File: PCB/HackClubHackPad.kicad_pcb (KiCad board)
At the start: 2 copper layers, 59.1 x 47 mm, 7 parts, among them J1 Conn_01x04, SW1 SW_Push, SW2 SW_Push, SW3 SW_Push, SW4 RotaryEncoder_Switch, SW5 RotaryEncoder_Switch, U1 Seeed Studio XIAO SAMD21

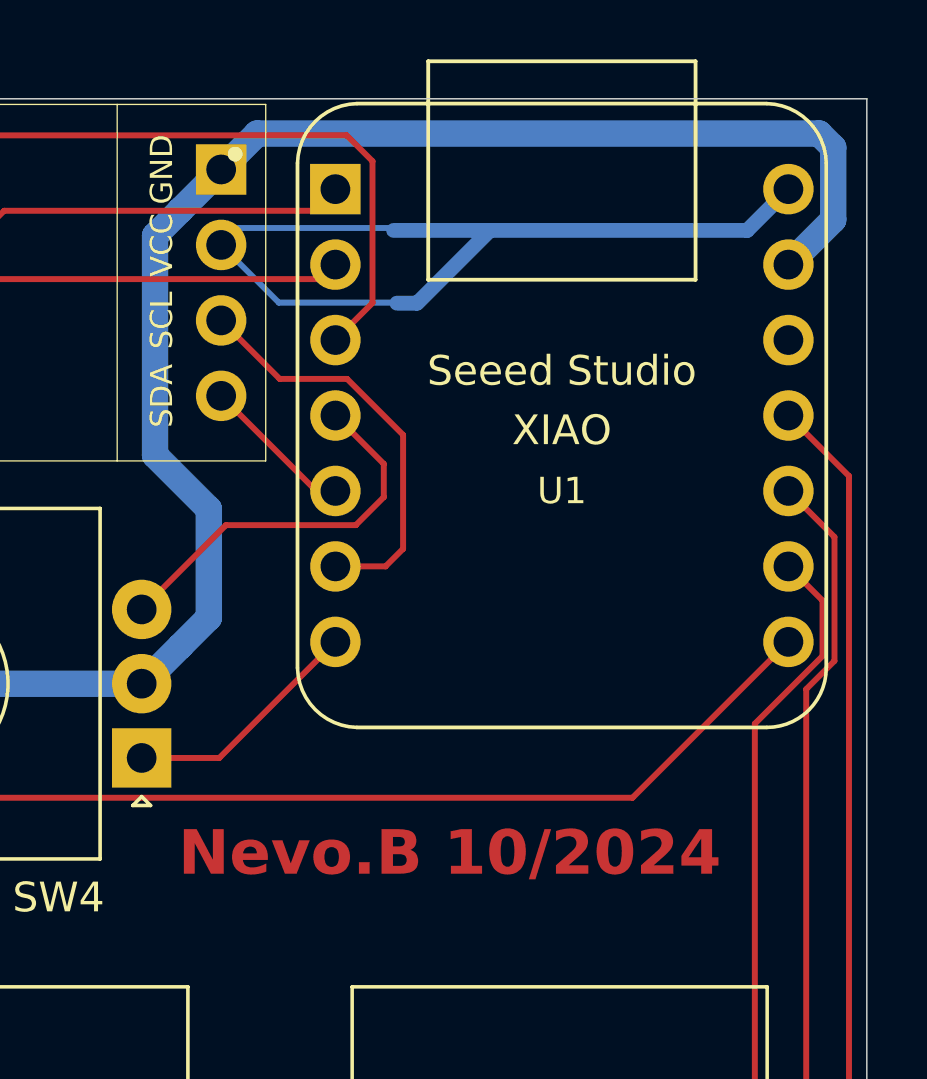
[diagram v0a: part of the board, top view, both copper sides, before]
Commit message: fixed firmware and changed pcb a bit
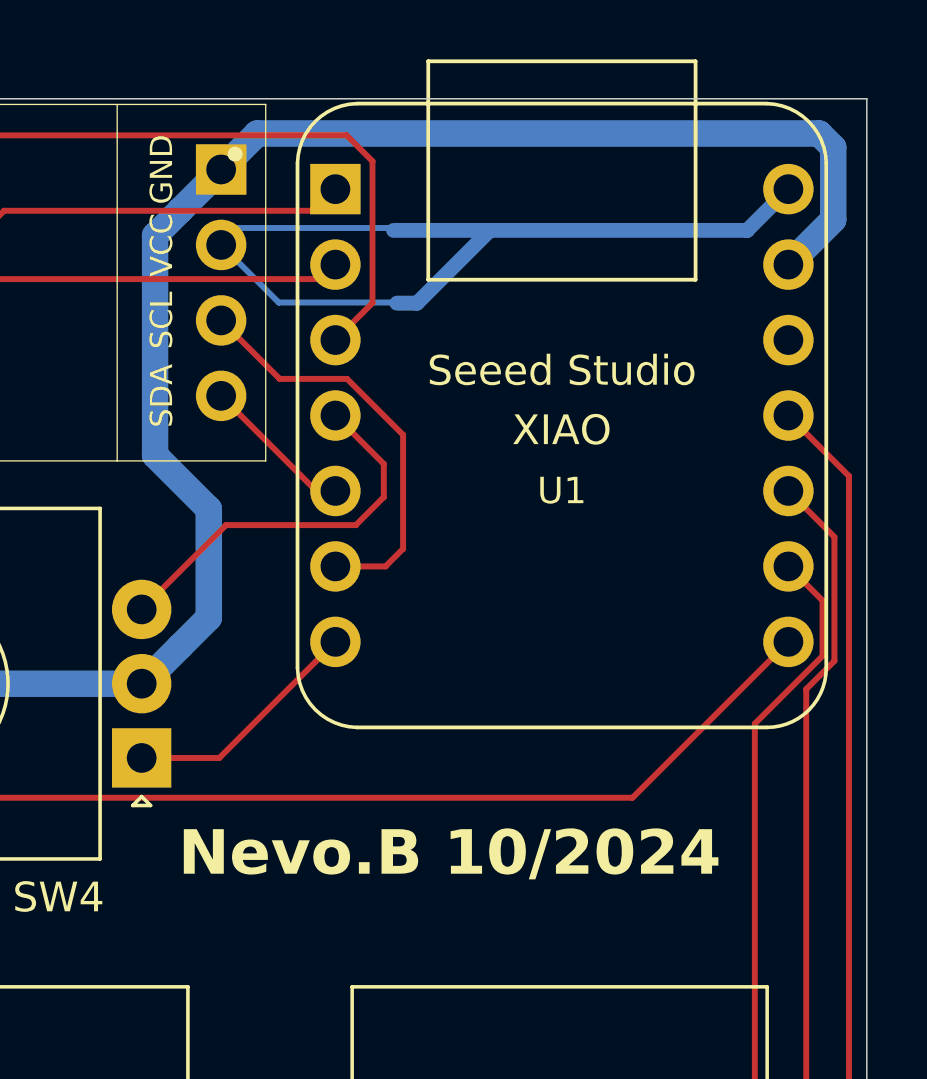
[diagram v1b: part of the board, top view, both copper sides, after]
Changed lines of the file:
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@@
 		(tags "rotary encoder")
 		(property "Reference" "SW5"
-			(at 2.8 -4.7 360)
+			(at 2.8 -4.7 0)
 			(layer "F.SilkS")
 			(effects
@@
 		)
 		(property "Value" "RotaryEncoder_Switch"
-			(at 7.5 10.4 360)
+			(at 7.5 10.4 0)
 			(layer "F.Fab")
 			(effects
@@
 		)
 		(fp_text user "${REFERENCE}"
-			(at 11.1 6.3 360)
+			(at 11.1 6.3 0)
 			(layer "F.Fab")
 			(effects
@@
 		(at 178.64525 33.422015)
 		(property "Reference" "U1"
-			(at 0 2.54 360)
+			(at 0 2.54 0)
 			(layer "F.SilkS")
 			(effects
@@
 		)
 		(property "Value" "Seeed Studio XIAO SAMD21"
-			(at 0 5.08 360)
+			(at 0 5.08 0)
 			(layer "F.SilkS")
 			(hide yes)
@@
 		)
 		(property "Footprint" "Seeed Studio XIAO Series Library:XIAO-Generic-Thruhole-14P-2.54-21X17.8MM"
-			(at 0 0 360)
+			(at 0 0 0)
 			(layer "F.Fab")
 			(hide yes)
@@
 		)
 		(property "Datasheet" ""
-			(at 0 0 360)
+			(at 0 0 0)
 			(layer "F.Fab")
 			(hide yes)
@@
 		)
 		(property "Description" ""
-			(at 0 0 360)
+			(at 0 0 0)
 			(layer "F.Fab")
 			(hide yes)
@@
 		(fp_arc
 			(start 6.9 -10.5)
-			(mid 8.301492 -9.901492)
+			(mid 8.301494 -9.901494)
 			(end 8.9 -8.5)
 			(stroke
@@
 		(tags "Cherry MX keyswitch 1.00u PCB")
 		(property "Reference" "SW1"
-			(at -2.54 -2.794 360)
+			(at -2.54 -2.794 0)
 			(layer "F.SilkS")
 			(effects
@@
 		)
 		(property "Value" "SW_Push"
-			(at -2.54 12.954 360)
+			(at -2.54 12.954 0)
 			(layer "F.Fab")
 			(effects
@@
 		)
 		(fp_text user "${REFERENCE}"
-			(at -2.54 -2.794 360)
+			(at -2.54 -2.794 0)
 			(layer "F.Fab")
 			(effects
@@
 		(tags "rotary encoder")
 		(property "Reference" "SW4"
-			(at 2.8 -4.7 360)
+			(at 2.8 -4.7 0)
 			(layer "F.SilkS")
 			(effects
@@
 		)
 		(property "Value" "RotaryEncoder_Switch"
-			(at 7.5 10.4 360)
+			(at 7.5 10.4 0)
 			(layer "F.Fab")
 			(effects
@@
 		)
 		(fp_text user "${REFERENCE}"
-			(at 11.1 6.3 360)
+			(at 11.1 6.3 0)
 			(layer "F.Fab")
 			(effects
@@
 		(tags "Cherry MX keyswitch 1.00u PCB")
 		(property "Reference" "SW3"
-			(at -2.54 -2.794 360)
+			(at -2.54 -2.794 0)
 			(layer "F.SilkS")
 			(effects
@@
 		)
 		(property "Value" "SW_Push"
-			(at -2.54 12.954 360)
+			(at -2.54 12.954 0)
 			(layer "F.Fab")
 			(effects
@@
 		)
 		(fp_text user "${REFERENCE}"
-			(at -2.54 -2.794 360)
+			(at -2.54 -2.794 0)
 			(layer "F.Fab")
 			(effects
@@
 		(tags "Cherry MX keyswitch 1.00u PCB")
 		(property "Reference" "SW2"
-			(at -2.54 -2.794 360)
+			(at -2.54 -2.794 0)
 			(layer "F.SilkS")
 			(effects
@@
 		)
 		(property "Value" "SW_Push"
-			(at -2.54 12.954 360)
+			(at -2.54 12.954 0)
 			(layer "F.Fab")
 			(effects
@@
 		)
 		(fp_text user "${REFERENCE}"
-			(at -2.54 -2.794 360)
+			(at -2.54 -2.794 0)
 			(layer "F.Fab")
 			(effects
@@
 	(gr_text "Nevo.B 10/2024"
 		(at 165.73 49.03 0)
-		(layer "F.Cu")
+		(layer "F.SilkS")
 		(effects
 			(font
